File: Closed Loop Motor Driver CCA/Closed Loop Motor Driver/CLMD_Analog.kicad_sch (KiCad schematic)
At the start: 15 parts, among them U3 MCP3208-CI_SL, U4 ACS712xLCTR-05B, U5 TXB0104D, U6 MCP1501-40xSN

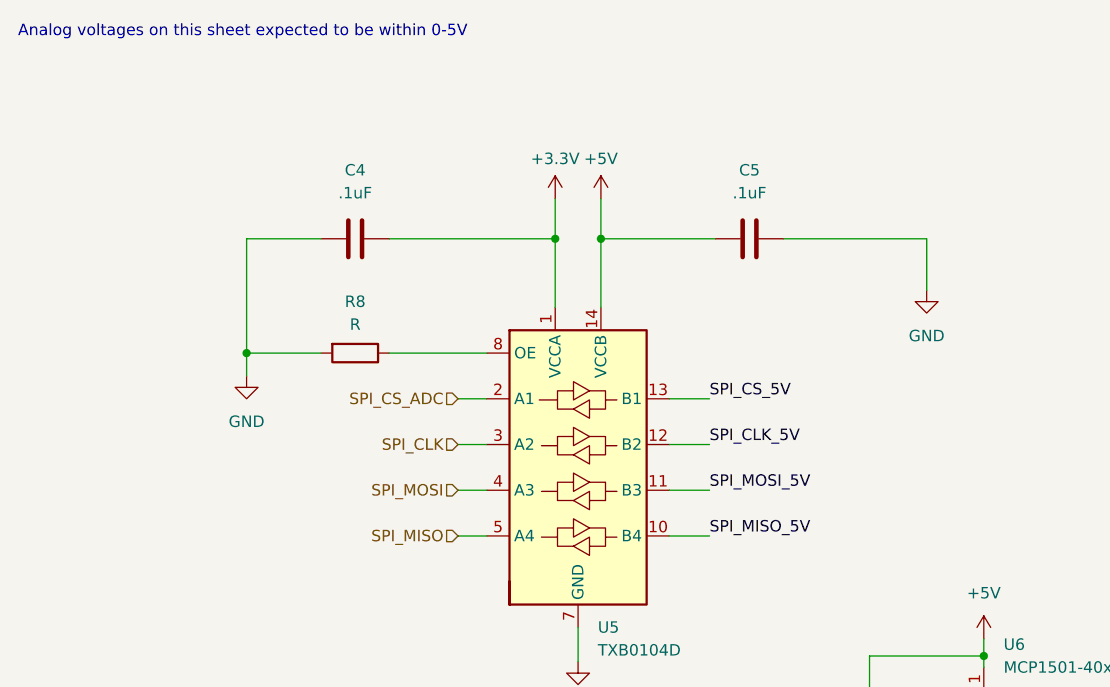
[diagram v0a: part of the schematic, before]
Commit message: collected unused signals into connectors
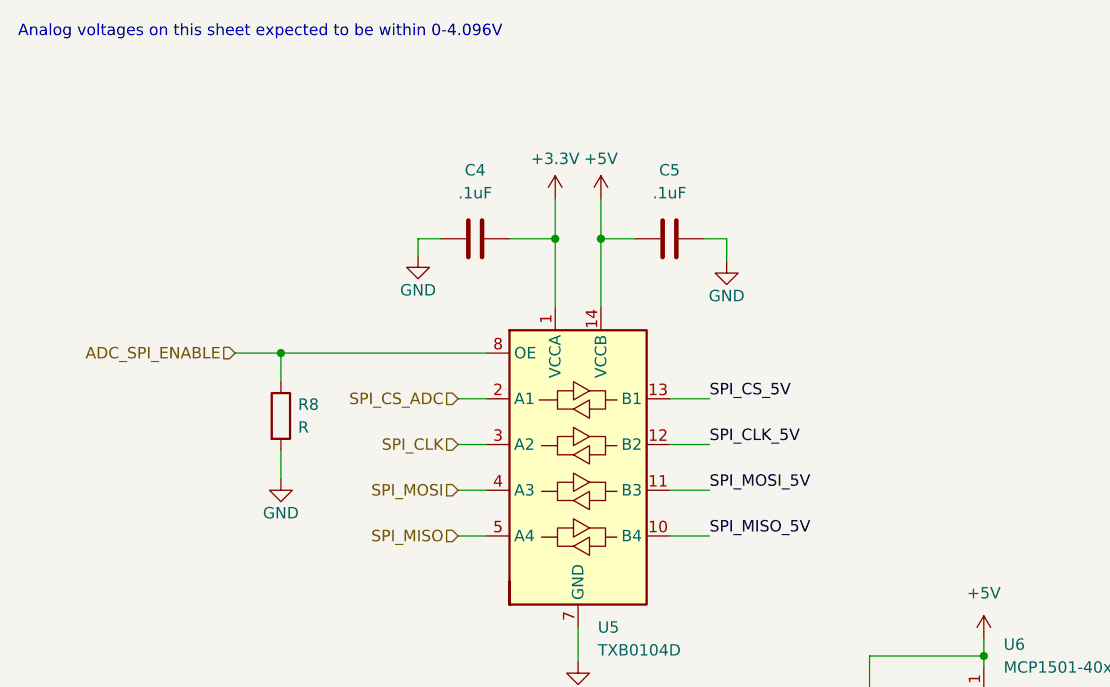
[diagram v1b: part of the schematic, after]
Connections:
- net ADC_SPI_ENABLE: now reaches R8.1, U5.8 (OE)
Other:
- note added: "Analog voltages on this sheet expected to be within 0-4.096V"
- note removed: "Analog voltages on this sheet expected to be within 0-5V"
- moved on the sheet: C4, C5, R8
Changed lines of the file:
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@@
   (junction (at 120.015 100.965) (diameter 0) (color 0 0 0 0)
   )
-  (junction (at 38.1 49.53) (diameter 0) (color 0 0 0 0)
-  )
   (junction (at 120.015 83.185) (diameter 0) (color 0 0 0 0)
   )
+  (junction (at 41.91 49.53) (diameter 0) (color 0 0 0 0)
+  )
   (junction (at 156.845 142.24) (diameter 0) (color 0 0 0 0)
   )
@@
     (stroke (width 0) (type default))
   )
-  (wire (pts (xy 46.355 36.83) (xy 38.1 36.83))
+  (wire (pts (xy 59.69 36.83) (xy 57.15 36.83))
     (stroke (width 0) (type default))
   )
@@
     (stroke (width 0) (type default))
   )
-  (wire (pts (xy 38.1 49.53) (xy 38.1 52.07))
-    (stroke (width 0) (type default))
-  )
   (wire (pts (xy 156.845 114.935) (xy 156.845 120.65))
     (stroke (width 0) (type default))
@@
     (stroke (width 0) (type default))
   )
+  (wire (pts (xy 64.77 49.53) (xy 41.91 49.53))
+    (stroke (width 0) (type default))
+  )
   (wire (pts (xy 61.595 69.85) (xy 64.77 69.85))
     (stroke (width 0) (type default))
   )
-  (wire (pts (xy 53.975 49.53) (xy 64.77 49.53))
-    (stroke (width 0) (type default))
-  )
   (wire (pts (xy 120.015 100.965) (xy 120.015 99.695))
     (stroke (width 0) (type default))
@@
     (stroke (width 0) (type default))
   )
-  (wire (pts (xy 53.975 36.83) (xy 72.39 36.83))
+  (wire (pts (xy 67.31 36.83) (xy 72.39 36.83))
     (stroke (width 0) (type default))
   )
@@
     (stroke (width 0) (type default))
   )
-  (wire (pts (xy 38.1 36.83) (xy 38.1 49.53))
+  (wire (pts (xy 57.15 36.83) (xy 57.15 38.735))
     (stroke (width 0) (type default))
   )
@@
     (stroke (width 0) (type default))
   )
-  (wire (pts (xy 46.355 49.53) (xy 38.1 49.53))
-    (stroke (width 0) (type default))
-  )
-  (wire (pts (xy 113.665 36.83) (xy 113.665 42.545))
+  (wire (pts (xy 41.91 49.53) (xy 41.91 52.705))
+    (stroke (width 0) (type default))
+  )
+  (wire (pts (xy 91.44 36.83) (xy 91.44 39.37))
     (stroke (width 0) (type default))
   )
@@
     (stroke (width 0) (type default))
   )
+  (wire (pts (xy 36.83 49.53) (xy 41.91 49.53))
+    (stroke (width 0) (type default))
+  )
   (wire (pts (xy 166.37 69.215) (xy 170.815 69.215))
     (stroke (width 0) (type default))
@@
     (stroke (width 0) (type default))
   )
-  (wire (pts (xy 97.79 36.83) (xy 113.665 36.83))
+  (wire (pts (xy 91.44 36.83) (xy 88.9 36.83))
     (stroke (width 0) (type default))
   )
@@
     (stroke (width 0) (type default))
   )
+  (wire (pts (xy 41.91 60.325) (xy 41.91 63.5))
+    (stroke (width 0) (type default))
+  )
   (wire (pts (xy 85.09 69.85) (xy 89.535 69.85))
     (stroke (width 0) (type default))
@@
     (stroke (width 0) (type default))
   )
-  (wire (pts (xy 77.47 36.83) (xy 90.17 36.83))
+  (wire (pts (xy 77.47 36.83) (xy 81.28 36.83))
     (stroke (width 0) (type default))
   )
@@
     (fill (type none))
   )
-  (text "Analog voltages on this sheet expected to be within 0-5V"
+  (text "Analog voltages on this sheet expected to be within 0-4.096V"
     (at 12.7 14.605 0)
     (effects (font (size 1.27 1.27)) (justify left bottom))
@@
     (effects (font (size 1.27 1.27)) (justify right))
   )
+  (hierarchical_label "ADC_SPI_ENABLE" (shape input) (at 36.83 49.53 180) (fields_autoplaced)
+    (effects (font (size 1.27 1.27)) (justify right))
+  )
   (hierarchical_label "A-IN_EXTRA_3" (shape input) (at 166.37 81.915 180) (fields_autoplaced)
     (effects (font (size 1.27 1.27)) (justify right))
@@
     )
   )
-  (symbol (lib_id "Device:C") (at 93.98 36.83 90) (unit 1)
-    (in_bom yes) (on_board yes) (dnp no) (fields_autoplaced)
-    (property "Reference" "C5" (at 93.98 29.21 90)
-      (effects (font (size 1.27 1.27)))
-    )
-    (property "Value" ".1uF" (at 93.98 31.75 90)
-      (effects (font (size 1.27 1.27)))
-    )
-    (property "Footprint" "" (at 97.79 35.8648 0)
-      (effects (font (size 1.27 1.27)) hide)
-    )
-    (property "Datasheet" "~" (at 93.98 36.83 0)
+  (symbol (lib_id "Device:C") (at 85.09 36.83 90) (unit 1)
+    (in_bom yes) (on_board yes) (dnp no) (fields_autoplaced)
+    (property "Reference" "C5" (at 85.09 29.21 90)
+      (effects (font (size 1.27 1.27)))
+    )
+    (property "Value" ".1uF" (at 85.09 31.75 90)
+      (effects (font (size 1.27 1.27)))
+    )
+    (property "Footprint" "" (at 88.9 35.8648 0)
+      (effects (font (size 1.27 1.27)) hide)
+    )
+    (property "Datasheet" "~" (at 85.09 36.83 0)
       (effects (font (size 1.27 1.27)) hide)
     )
@@
     )
   )
-  (symbol (lib_id "Device:C") (at 50.165 36.83 90) (unit 1)
-    (in_bom yes) (on_board yes) (dnp no) (fields_autoplaced)
-    (property "Reference" "C4" (at 50.165 29.21 90)
-      (effects (font (size 1.27 1.27)))
-    )
-    (property "Value" ".1uF" (at 50.165 31.75 90)
-      (effects (font (size 1.27 1.27)))
-    )
-    (property "Footprint" "" (at 53.975 35.8648 0)
-      (effects (font (size 1.27 1.27)) hide)
-    )
-    (property "Datasheet" "~" (at 50.165 36.83 0)
+  (symbol (lib_id "Device:C") (at 63.5 36.83 90) (unit 1)
+    (in_bom yes) (on_board yes) (dnp no) (fields_autoplaced)
+    (property "Reference" "C4" (at 63.5 29.21 90)
+      (effects (font (size 1.27 1.27)))
+    )
+    (property "Value" ".1uF" (at 63.5 31.75 90)
+      (effects (font (size 1.27 1.27)))
+    )
+    (property "Footprint" "" (at 67.31 35.8648 0)
+      (effects (font (size 1.27 1.27)) hide)
+    )
+    (property "Datasheet" "~" (at 63.5 36.83 0)
       (effects (font (size 1.27 1.27)) hide)
     )
@@
     )
   )
-  (symbol (lib_id "power:GND") (at 113.665 42.545 0) (unit 1)
-    (in_bom yes) (on_board yes) (dnp no) (fields_autoplaced)
-    (property "Reference" "#PWR024" (at 113.665 48.895 0)
-      (effects (font (size 1.27 1.27)) hide)
-    )
-    (property "Value" "GND" (at 113.665 47.625 0)
-      (effects (font (size 1.27 1.27)))
-    )
-    (property "Footprint" "" (at 113.665 42.545 0)
-      (effects (font (size 1.27 1.27)) hide)
-    )
-    (property "Datasheet" "" (at 113.665 42.545 0)
+  (symbol (lib_id "power:GND") (at 91.44 39.37 0) (unit 1)
+    (in_bom yes) (on_board yes) (dnp no)
+    (property "Reference" "#PWR024" (at 91.44 45.72 0)
+      (effects (font (size 1.27 1.27)) hide)
+    )
+    (property "Value" "GND" (at 91.44 43.18 0)
+      (effects (font (size 1.27 1.27)))
+    )
+    (property "Footprint" "" (at 91.44 39.37 0)
+      (effects (font (size 1.27 1.27)) hide)
+    )
+    (property "Datasheet" "" (at 91.44 39.37 0)
       (effects (font (size 1.27 1.27)) hide)
     )
@@
         (path "/476d0229-4bfd-469e-978e-c7776793cea2/5a8866ce-a8b7-4035-83e2-5723f6b2be5e"
           (reference "R5") (unit 1)
+        )
+      )
+    )
+  )
+  (symbol (lib_id "power:GND") (at 41.91 63.5 0) (unit 1)
+    (in_bom yes) (on_board yes) (dnp no)
+    (property "Reference" "#PWR040" (at 41.91 69.85 0)
+      (effects (font (size 1.27 1.27)) hide)
+    )
+    (property "Value" "GND" (at 41.91 67.31 0)
+      (effects (font (size 1.27 1.27)))
+    )
+    (property "Footprint" "" (at 41.91 63.5 0)
+      (effects (font (size 1.27 1.27)) hide)
+    )
+    (property "Datasheet" "" (at 41.91 63.5 0)
+      (effects (font (size 1.27 1.27)) hide)
+    )
+    (pin "1")
+    (instances
+      (project "Closed Loop Motor Driver"
+        (path "/476d0229-4bfd-469e-978e-c7776793cea2/5a8866ce-a8b7-4035-83e2-5723f6b2be5e"
+          (reference "#PWR040") (unit 1)
         )
       )
@@
     )
   )
-  (symbol (lib_id "power:GND") (at 38.1 52.07 0) (unit 1)
-    (in_bom yes) (on_board yes) (dnp no) (fields_autoplaced)
-    (property "Reference" "#PWR023" (at 38.1 58.42 0)
-      (effects (font (size 1.27 1.27)) hide)
-    )
-    (property "Value" "GND" (at 38.1 57.15 0)
-      (effects (font (size 1.27 1.27)))
-    )
-    (property "Footprint" "" (at 38.1 52.07 0)
-      (effects (font (size 1.27 1.27)) hide)
-    )
-    (property "Datasheet" "" (at 38.1 52.07 0)
+  (symbol (lib_id "power:GND") (at 57.15 38.735 0) (unit 1)
+    (in_bom yes) (on_board yes) (dnp no)
+    (property "Reference" "#PWR023" (at 57.15 45.085 0)
+      (effects (font (size 1.27 1.27)) hide)
+    )
+    (property "Value" "GND" (at 57.15 42.545 0)
+      (effects (font (size 1.27 1.27)))
+    )
+    (property "Footprint" "" (at 57.15 38.735 0)
+      (effects (font (size 1.27 1.27)) hide)
+    )
+    (property "Datasheet" "" (at 57.15 38.735 0)
       (effects (font (size 1.27 1.27)) hide)
     )
@@
     )
   )
-  (symbol (lib_id "Device:R") (at 50.165 49.53 270) (unit 1)
-    (in_bom yes) (on_board yes) (dnp no) (fields_autoplaced)
-    (property "Reference" "R8" (at 50.165 43.815 90)
-      (effects (font (size 1.27 1.27)))
-    )
-    (property "Value" "R" (at 50.165 46.355 90)
-      (effects (font (size 1.27 1.27)))
-    )
-    (property "Footprint" "" (at 50.165 47.752 90)
-      (effects (font (size 1.27 1.27)) hide)
-    )
-    (property "Datasheet" "~" (at 50.165 49.53 0)
-      (effects (font (size 1.27 1.27)) hide)
-    )
+  (symbol (lib_id "Device:R") (at 41.91 56.515 0) (unit 1)
+    (in_bom yes) (on_board yes) (dnp no) (fields_autoplaced)
+    (property "Reference" "R8" (at 43.815 55.245 0)
+      (effects (font (size 1.27 1.27)) (justify left))
+    )
+    (property "Value" "R" (at 43.815 57.785 0)
+      (effects (font (size 1.27 1.27)) (justify left))
+    )
+    (property "Footprint" "" (at 40.132 56.515 90)
+      (effects (font (size 1.27 1.27)) hide)
+    )
+    (property "Datasheet" "~" (at 41.91 56.515 0)
+      (effects (font (size 1.27 1.27)) hide)
+    )

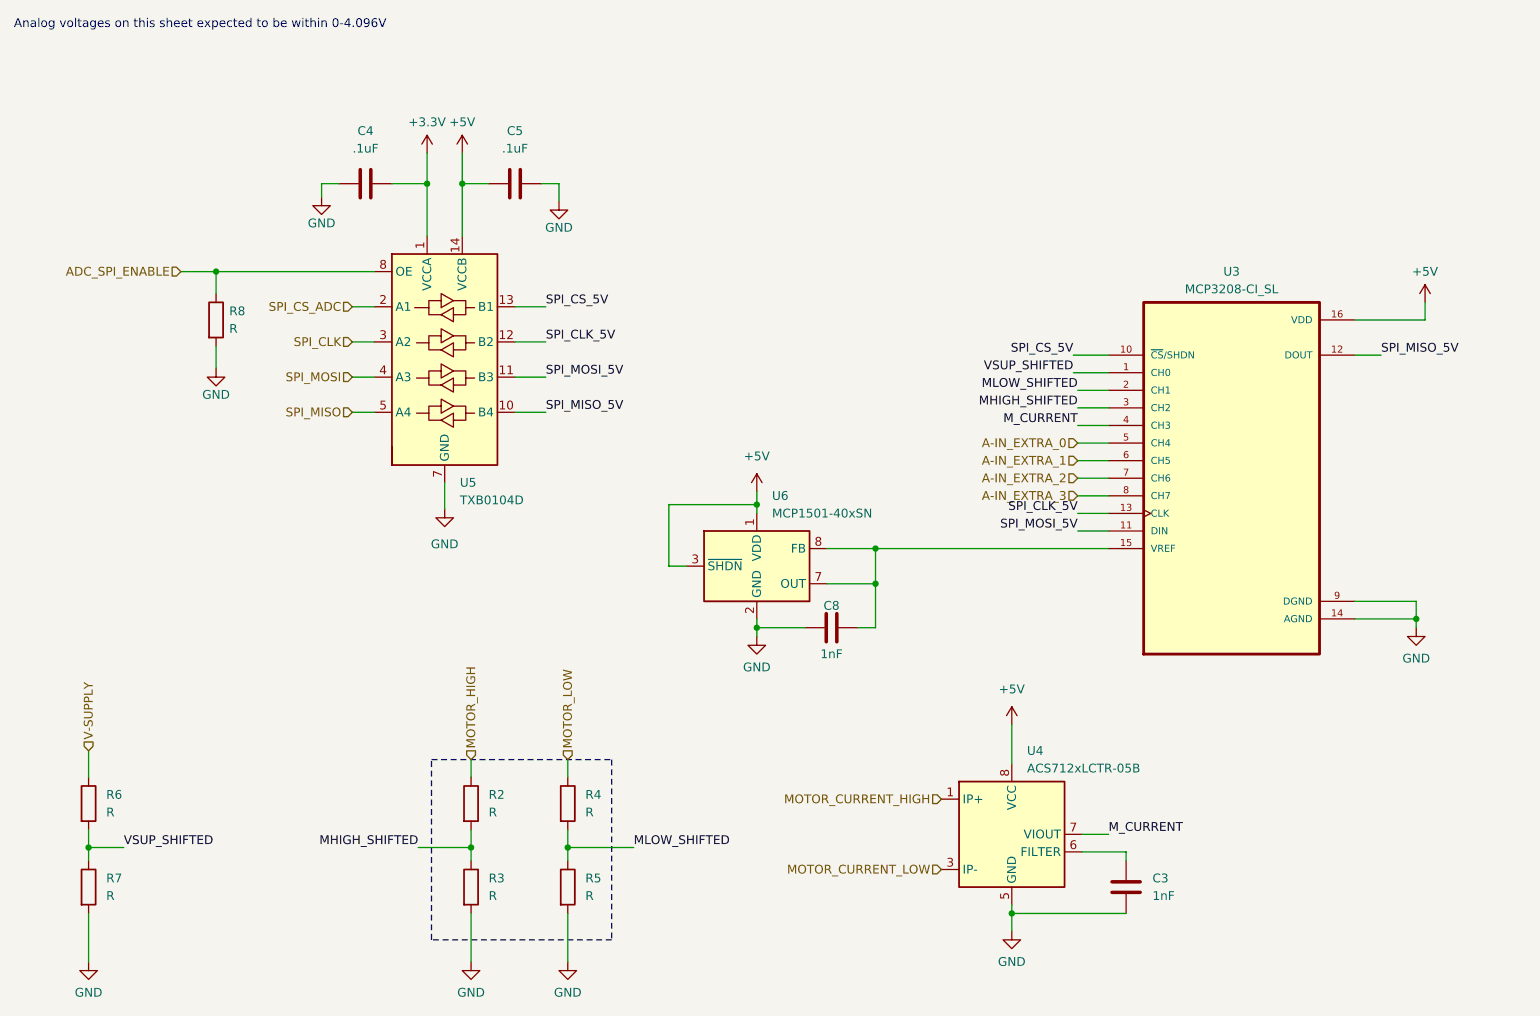
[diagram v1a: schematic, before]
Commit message: change gitignore for KiCAD
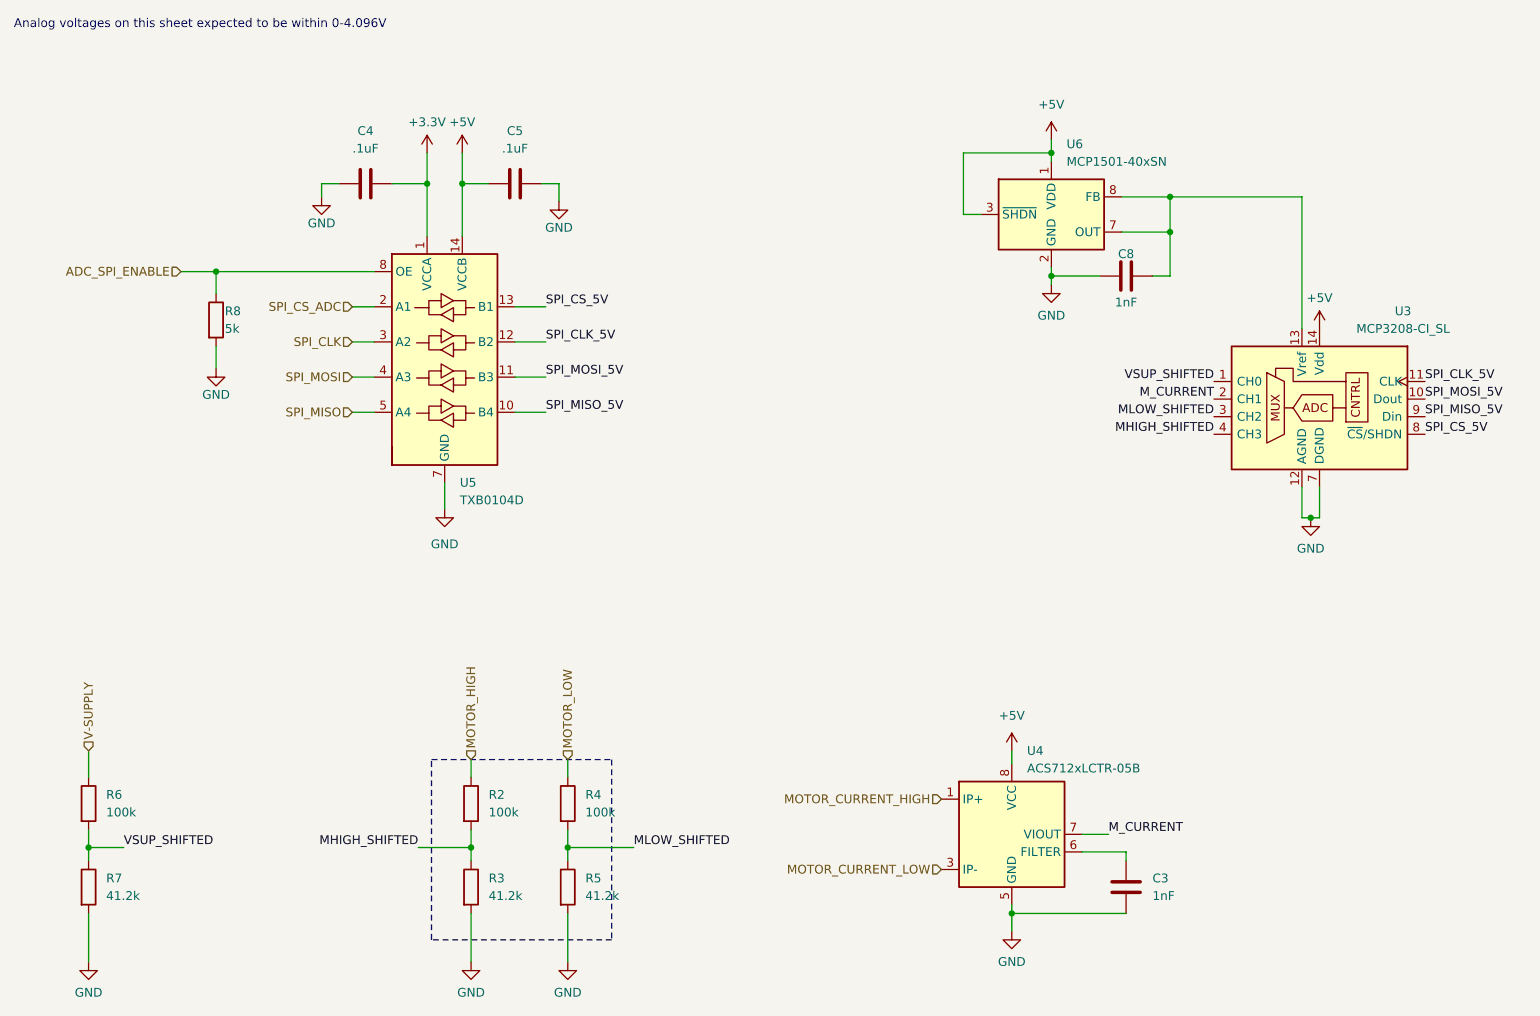
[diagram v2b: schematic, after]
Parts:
- R2, R4, R6: value R -> 100k
- R3, R5, R7: value R -> 41.2k
- R8: value R -> 5k; PART_NO (none) -> 1879246-3
- U3: symbol MCP3208-CI_SL:MCP3208-CI_SL -> Analog_ADC:MCP3204
- U6: PART_NO (none) -> MCP1501T-40E/SN
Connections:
- net A-IN_EXTRA_2 is gone; now on net GND: U3.7 (DGND)
- net A-IN_EXTRA_3 is gone; now on net SPI_CS_5V: U3.8 (~{CS}/SHDN)
- net +5V: now also U3.14 (Vdd); no longer U3.16 (VDD)
- net GND: now also U3.12 (AGND); no longer U3.14 (AGND), U3.9 (DGND)
- net MHIGH_SHIFTED: now also U3.4 (CH3); no longer U3.3 (CH2)
- net MLOW_SHIFTED: now also U3.3 (CH2); no longer U3.2 (CH1)
- net M_CURRENT: now also U3.2 (CH1); no longer U3.4 (CH3)
- net SPI_CLK_5V: now also U3.11 (CLK); no longer U3.13 (CLK)
- net SPI_CS_5V: no longer U3.10 (~{CS}/SHDN)
- net SPI_MISO_5V: now also U3.9 (Din); no longer U3.12 (DOUT)
- net SPI_MOSI_5V: now also U3.10 (Dout); no longer U3.11 (DIN)
- net at C8.2, U6.7 (OUT), U6.8 (FB): now also U3.13 (Vref); no longer U3.15 (VREF)
- net A-IN_EXTRA_0: no longer names the net of U3.5 (NC)
- net A-IN_EXTRA_1: no longer names the net of U3.6 (NC)
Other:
- moved on the sheet: C8, U6
